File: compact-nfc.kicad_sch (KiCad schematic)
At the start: 37 parts, among them Q1 2N7002, Q2 2N7002, U1 ITR9702, U2 PN5321A3HN_C1xx, Y1 Crystal_GND24

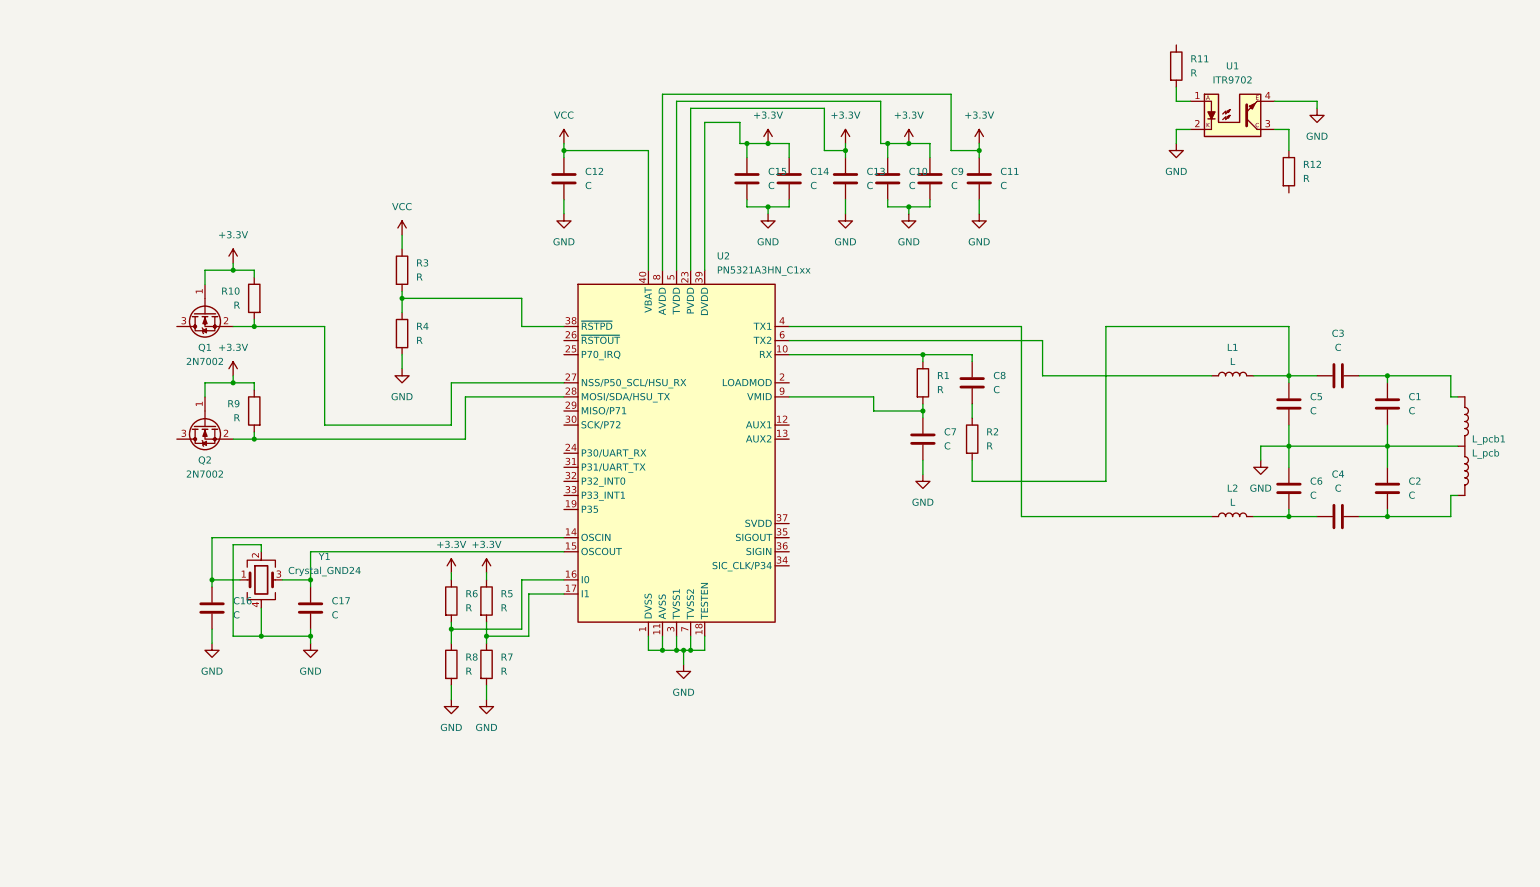
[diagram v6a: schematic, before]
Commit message: Add debug connector and start manual routing of critical RF coupling network sections
- Added debug connector to schematic and PCB
- Started manual routing of critical RF coupling network components
- Updated footprint library table
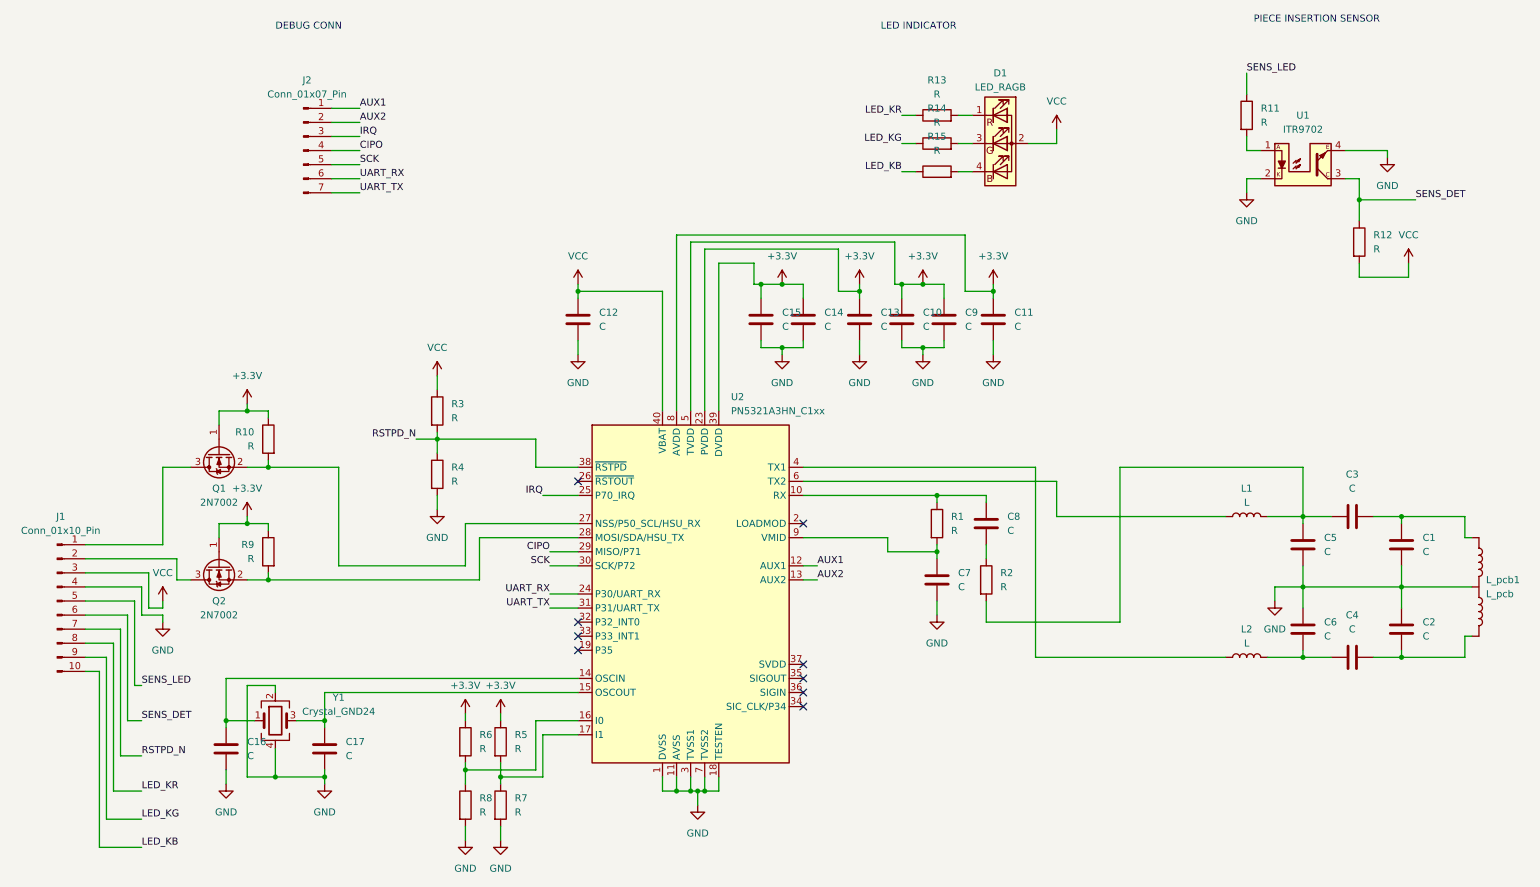
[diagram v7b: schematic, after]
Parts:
- added D1: LED_RAGB, LED_SMD_REVERSE_MOUNT:LED_RGB_SMD_6028_2.8x3.5mm_Square, symbol Device:LED_RAGB
- added J1: Conn_01x10_Pin, Connector_PinHeader_2.54mm:PinHeader_1x10_P2.54mm_Vertical, symbol Connector:Conn_01x10_Pin
- added J2: Conn_01x07_Pin, Connector_PinHeader_1.27mm:PinHeader_1x07_P1.27mm_Vertical, symbol Connector:Conn_01x07_Pin
- added R13, R14, R15: R, Resistor_SMD:R_0805_2012Metric_Pad1.20x1.40mm_HandSolder, symbol Device:R
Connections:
- net GND: now also J1.4 (Pin_4)
- net VCC: now also R12.2, D1.2 (A), J1.3 (Pin_3)
- net RSTPD_N: now reaches R3.2, R4.1, U2.38 (~{RSTPD})
- net RSTPD_N: now also J1.7 (Pin_7)
- net at Q1.3 (D): now also J1.1 (Pin_1)
- net AUX1: now reaches U2.12 (AUX1)
- net AUX1: now also J2.1 (Pin_1)
- net AUX2: now reaches U2.13 (AUX2)
- net AUX2: now also J2.2 (Pin_2)
- net UART_RX: now reaches U2.24 (P30/UART_RX)
- net UART_RX: now also J2.6 (Pin_6)
- net IRQ: now reaches U2.25 (P70_IRQ)
- net IRQ: now also J2.3 (Pin_3)
- net CIPO: now reaches U2.29 (MISO/P71)
- net CIPO: now also J2.4 (Pin_4)
- net SCK: now reaches U2.30 (SCK/P72)
- net SCK: now also J2.5 (Pin_5)
- net UART_TX: now reaches U2.31 (P31/UART_TX)
- net UART_TX: now also J2.7 (Pin_7)
- net SENS_DET: now reaches R12.1, U1.3
- net SENS_DET: now also J1.6 (Pin_6)
- net SENS_LED: now reaches R11.1
- net SENS_LED: now also J1.5 (Pin_5)
- net at Q2.3 (D): now also J1.2 (Pin_2)
- new net: D1.1 (RK), R13.2
- new net: D1.3 (GK), R14.2
- new net: D1.4 (BK), R15.2
- new net LED_KB: J1.10 (Pin_10), R15.1
- new net LED_KG: J1.9 (Pin_9), R14.1
- new net LED_KR: J1.8 (Pin_8), R13.1
- no-connect marks 0 -> 9
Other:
- note added: "DEBUG CONN"
- note added: "LED INDICATOR"
- note added: "PIECE INSERTION SENSOR"
- moved on the sheet: C1, C10, C11, C12, C13, C14, C15, C16, C17, C2, C3, C4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

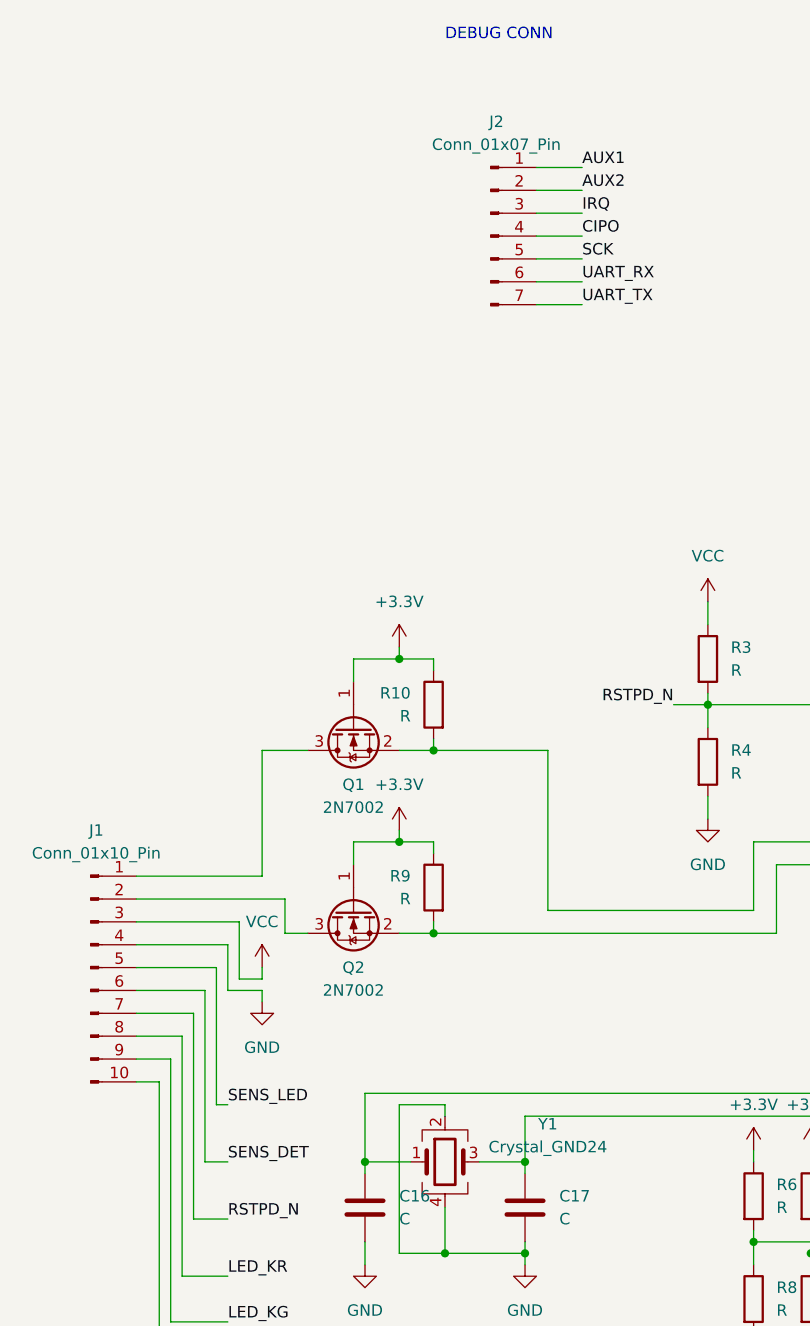
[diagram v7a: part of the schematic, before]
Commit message: Complete main trace routing
- Finished main trace routing for PCB layout
- Updated schematic and project files
- Updated backup files
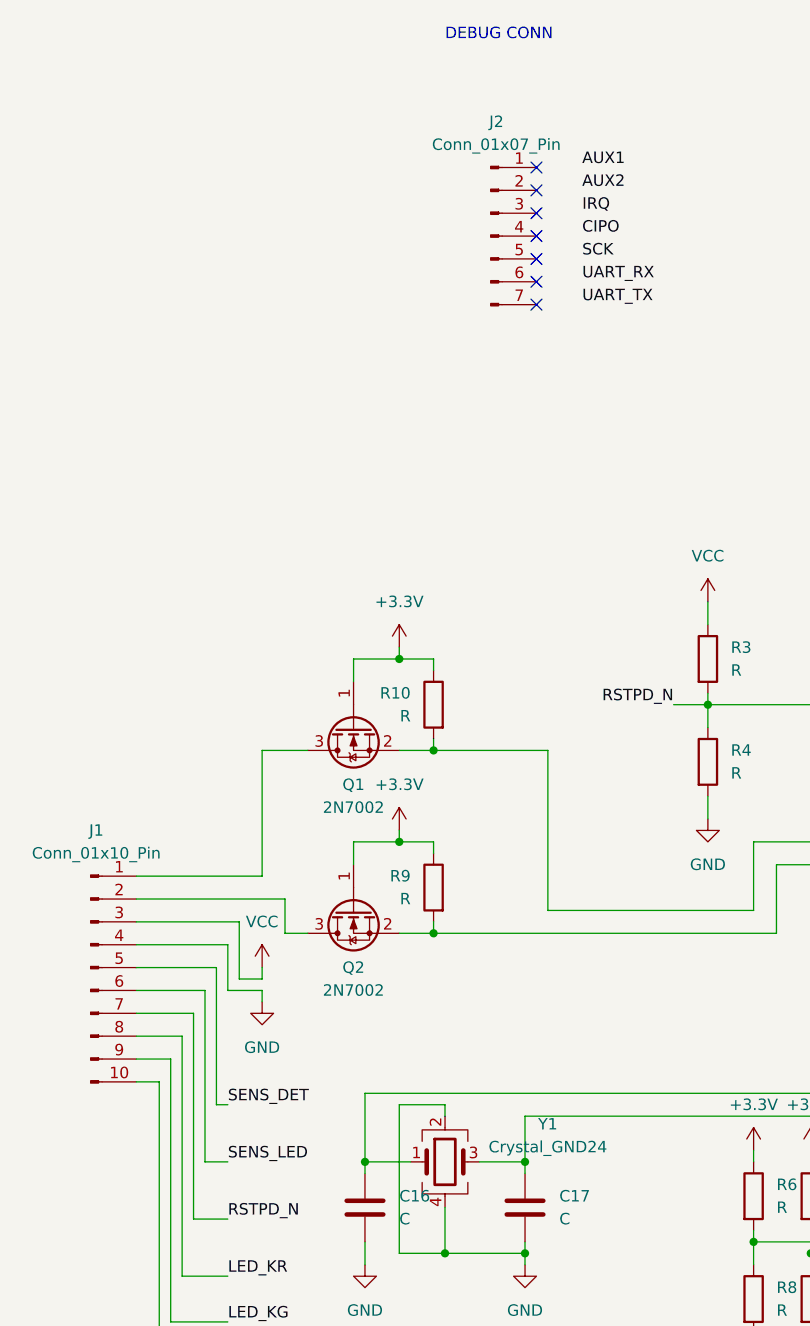
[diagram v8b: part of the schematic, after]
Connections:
- net AUX1: no longer J2.1 (Pin_1)
- net AUX2: no longer J2.2 (Pin_2)
- net CIPO: no longer J2.4 (Pin_4)
- net IRQ: no longer J2.3 (Pin_3)
- net SCK: no longer J2.5 (Pin_5)
- net SENS_DET: now also J1.5 (Pin_5); no longer J1.6 (Pin_6)
- net SENS_LED: now also J1.6 (Pin_6); no longer J1.5 (Pin_5)
- net UART_RX: no longer J2.6 (Pin_6)
- net UART_TX: no longer J2.7 (Pin_7)
- no-connect marks 9 -> 16
